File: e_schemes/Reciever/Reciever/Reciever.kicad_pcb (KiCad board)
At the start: 2 copper layers, 36 parts, among them J1 Conn_01x03, J2 Conn_01x03, SW1 SW_Push, SW2 SW_Push, SW3 SW_Reload, U1 ESP32-WROOM-32E

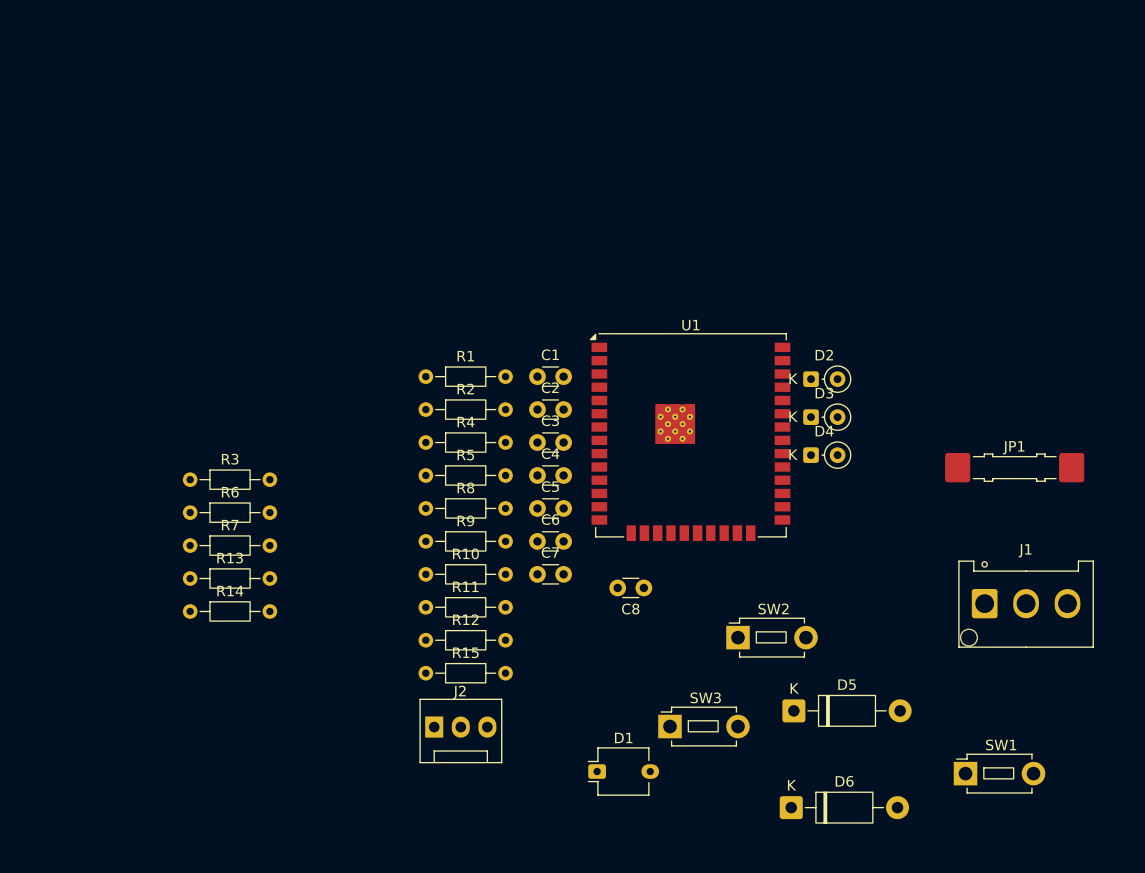
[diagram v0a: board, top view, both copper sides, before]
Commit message: Отрисовка схемы
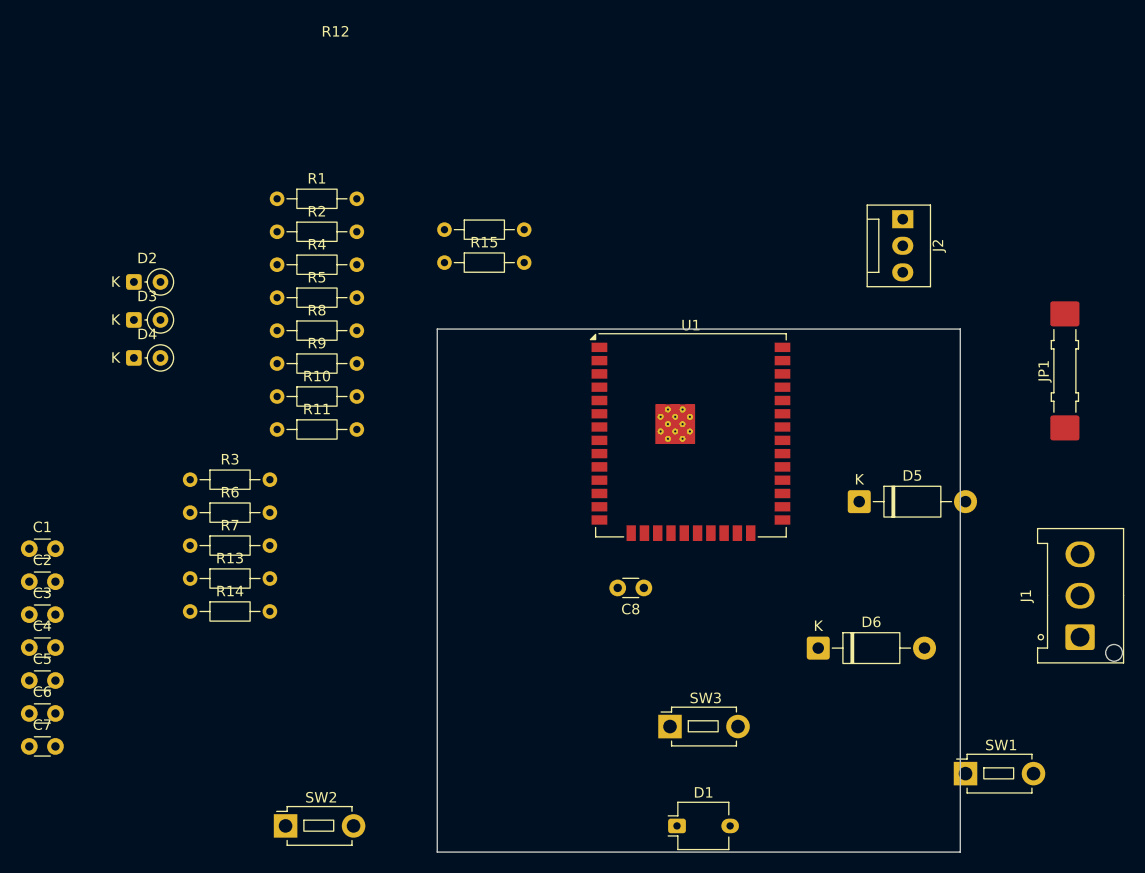
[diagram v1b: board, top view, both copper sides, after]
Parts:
- moved J2 66.1 mm to (140.5, 60.5), turned to -90 degrees
- moved D2 65.4 mm to (67.0, 66.5)
- moved D3 65.4 mm to (67.0, 70.1)
- moved D4 65.4 mm to (67.0, 73.8)
- moved C1 51.3 mm to (57.0, 92.0)
- moved C2 51.3 mm to (57.0, 95.2)
- moved C3 51.3 mm to (57.0, 98.3)
- moved C4 51.3 mm to (57.0, 101.5)
- moved C5 51.3 mm to (57.0, 104.6)
- moved C6 51.3 mm to (57.0, 107.8)
- moved C7 51.3 mm to (57.0, 110.9)
- moved SW2 46.8 mm to (81.5, 118.5)
- moved R12 39.3 mm to (96.7, 61.5)
- moved R15 39.3 mm to (96.7, 64.7)
- moved R1 22.2 mm to (80.7, 58.5)
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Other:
- board outline added: 50 x 50 mm
